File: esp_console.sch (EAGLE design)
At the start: 37 parts, among them IC1 74AHC1G04DBV, IC2 UA78M05DCY, J2 10118193-0001LF, Q1 12mhz, Q2 ON_SEMICONDUCTOR_BC849BLT1GON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, Q3 ON_SEMICONDUCTOR_BC849BLT1GON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, SW1 OS102011MA1Q

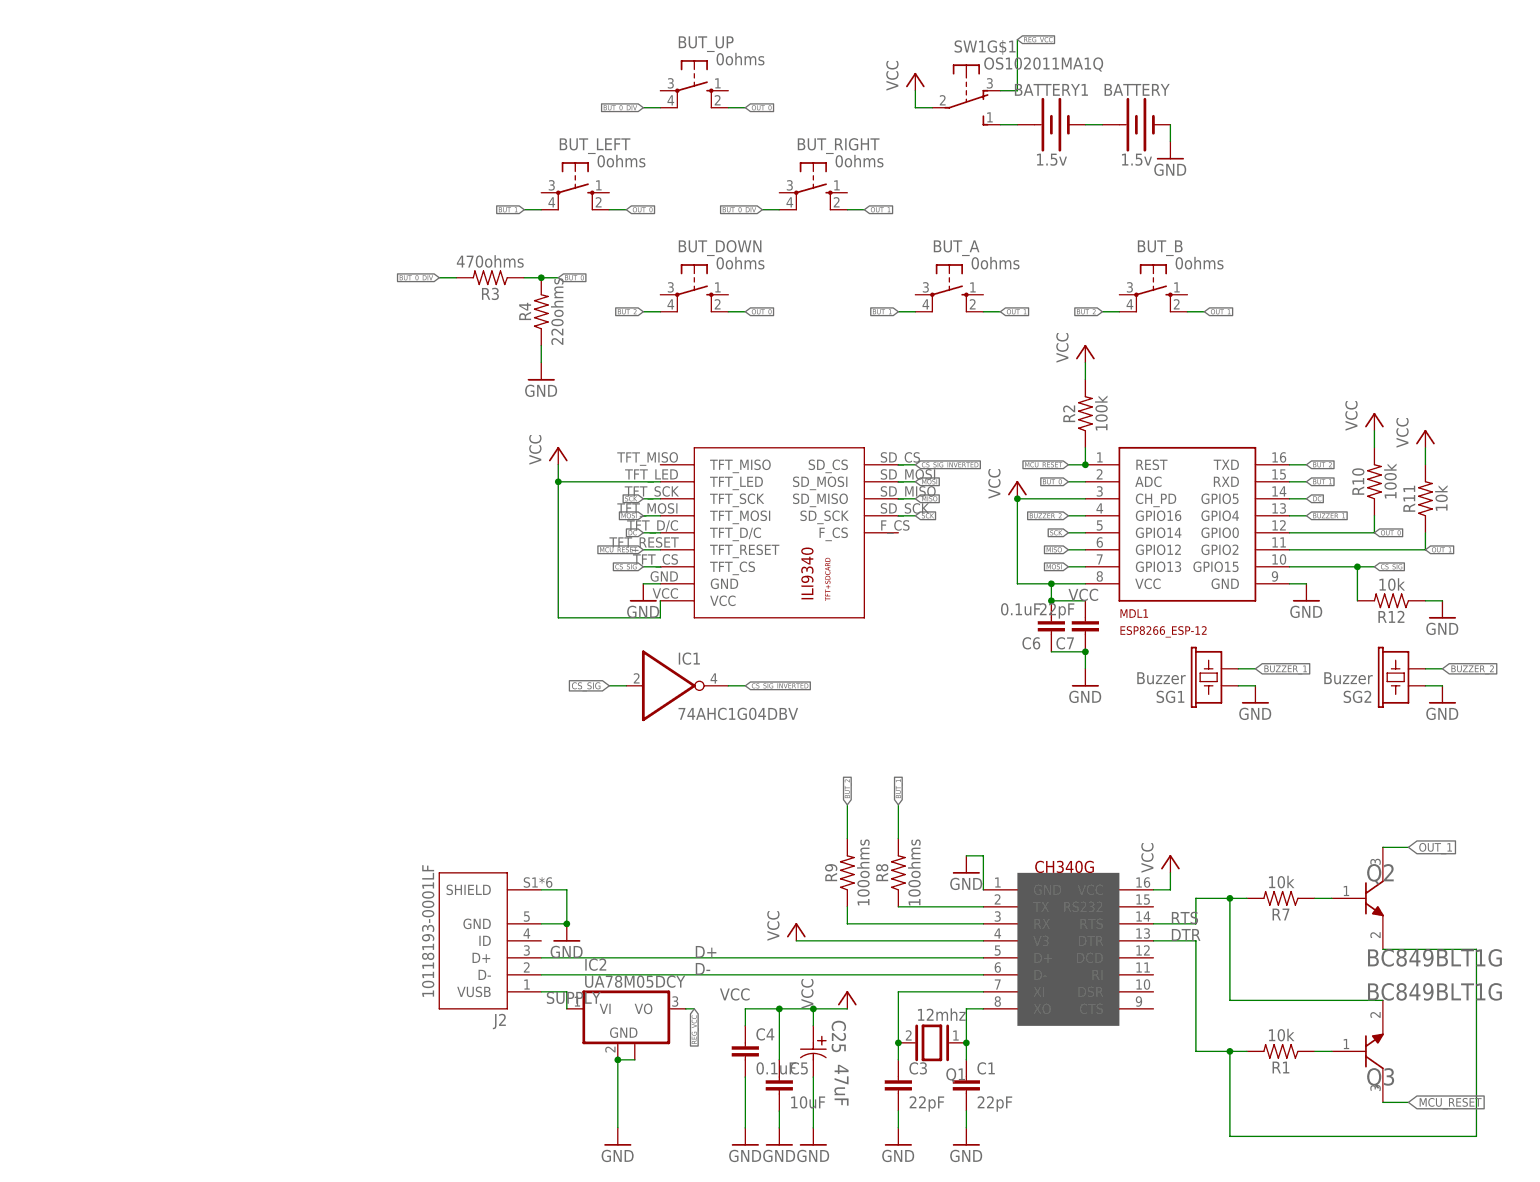
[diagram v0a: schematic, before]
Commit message: Updated design to 8 buttons
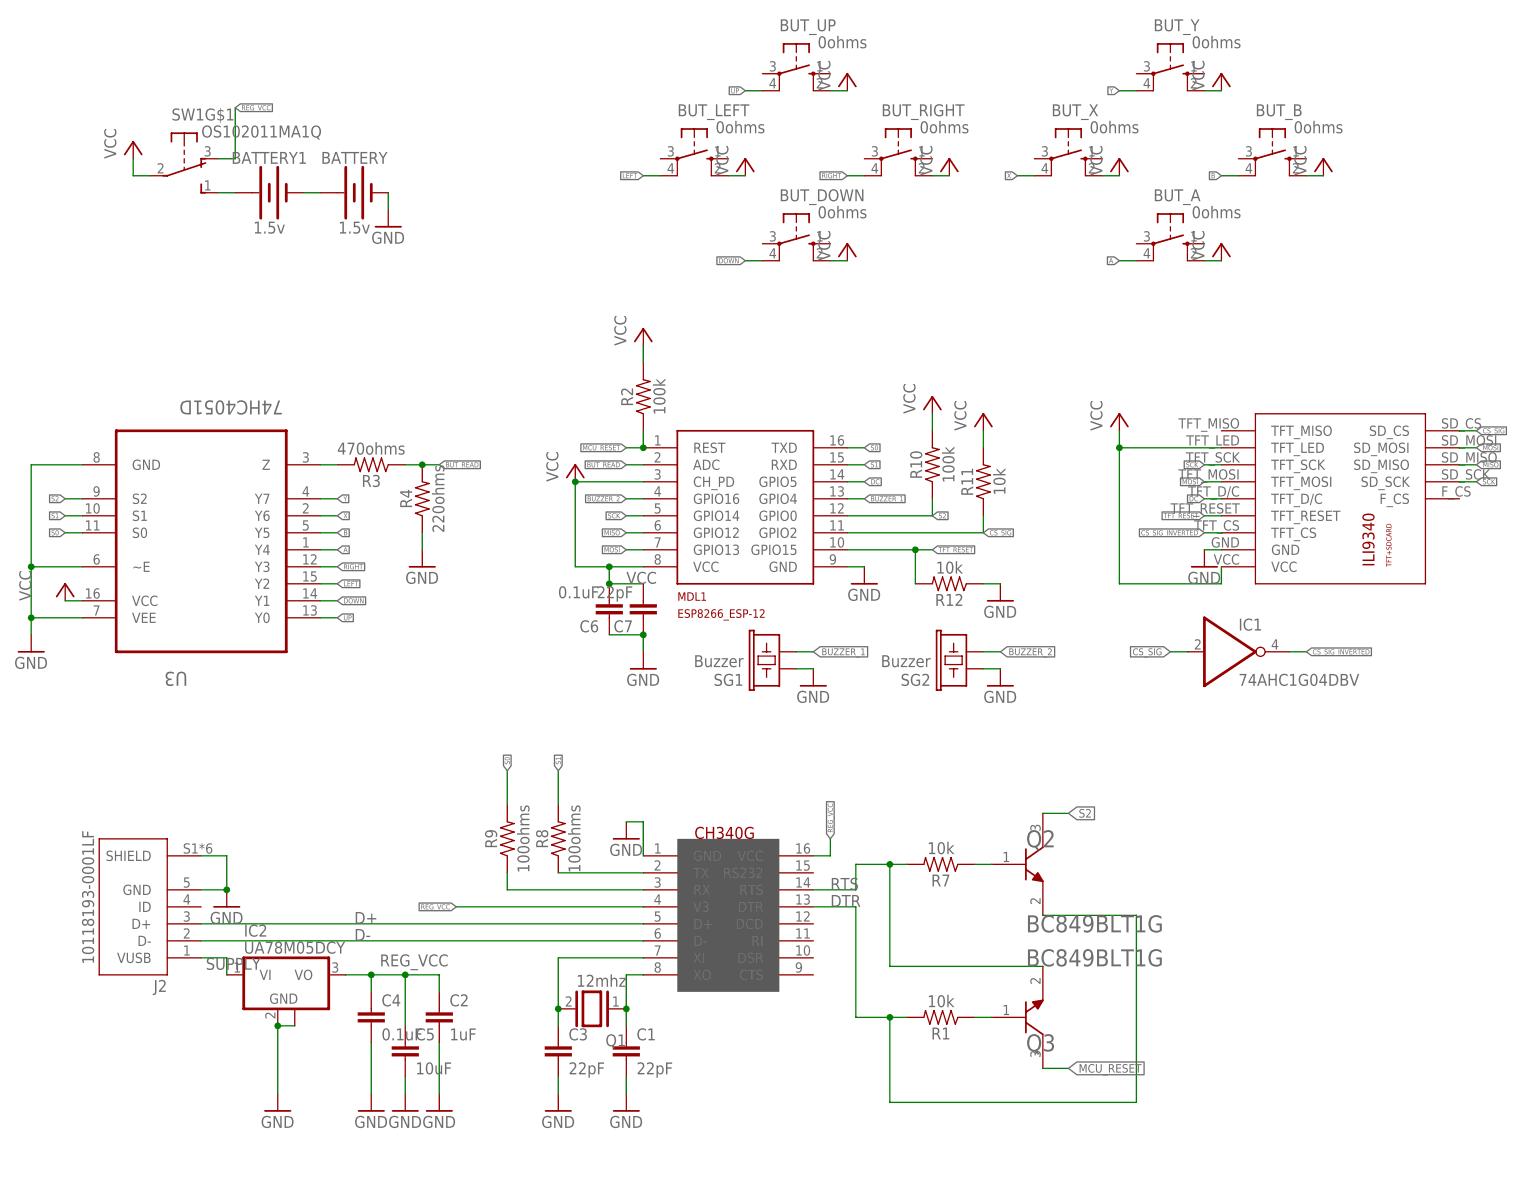
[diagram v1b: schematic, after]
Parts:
- removed C25: 47uF, Panasonic-EEEFK_EEEFP:EEE-FK1C471P-CASE-F
- added BUT_X, BUT_Y: 0ohms, switch-omron:10-XX
- added C2: 1uF, rcl:C-EUC0603
- added U3: 74HC4051D, 74HC4051D:74HC4051D
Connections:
- net BUT_0 renamed BUT_READ
- removed net BUT_0_DIV: BUT_RIGHT.P1, BUT_UP.P1, R3.2
- removed net BUT_1: BUT_A.P1, BUT_LEFT.P1, MDL1.RXD, R8.2
- removed net BUT_2: BUT_B.P1, BUT_DOWN.P1, MDL1.TXD, R9.2
- removed net OUT_0: BUT_DOWN.S1, BUT_LEFT.S1, BUT_UP.S1, MDL1.GPIO0, R10.1
- removed net OUT_1: BUT_A.S1, BUT_B.S1, BUT_RIGHT.S1, MDL1.GPIO2, Q2.C, R11.1
- new net A: BUT_A.P1, U3.Y4
- new net B: BUT_B.P1, U3.Y5
- new net BUT_READ_3V3: R3.2, U3.Z
- new net DOWN: BUT_DOWN.P1, U3.Y1
- new net LEFT: BUT_LEFT.P1, U3.Y2
- new net RIGHT: BUT_RIGHT.P1, U3.Y3
- new net S0: MDL1.TXD, R9.2, U3.S0
- new net S1: MDL1.RXD, R8.2, U3.S1
- new net S2: MDL1.GPIO0, Q2.C, R10.1, U3.S2
- new net TFT_RESET: MDL1.GPIO15, R12.2, U$2.TFT_RESET
- new net UP: BUT_UP.P1, U3.Y0
- new net X: BUT_X.P1, U3.Y6
- new net Y: BUT_Y.P1, U3.Y7
- net CS_SIG: now also MDL1.GPIO2, R11.1, U$2.SD_CS; no longer MDL1.GPIO15, R12.2, U$2.TFT_CS
- net CS_SIG_INVERTED: now also U$2.TFT_CS; no longer U$2.SD_CS
- net GND: now also C2.2, U3.GND, U3.VEE, U3.~E; no longer C25.2
- net MCU_RESET: no longer U$2.TFT_RESET
- net REG_VCC: now also C2.1, C4.1, C5.1, U$1.V3, U$1.VCC
- net VCC: now also BUT_A.S1, BUT_B.S1, BUT_DOWN.S1, BUT_LEFT.S1, BUT_RIGHT.S1, BUT_UP.S1, BUT_X.S1, BUT_Y.S1, U3.VCC; no longer C25.1, C4.1, C5.1, U$1.V3, U$1.VCC
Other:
- moved on the sheet: BATTERY, BATTERY1, BUT_A, BUT_B, BUT_DOWN, BUT_LEFT, BUT_RIGHT, BUT_UP, C1, C3, C4, C5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

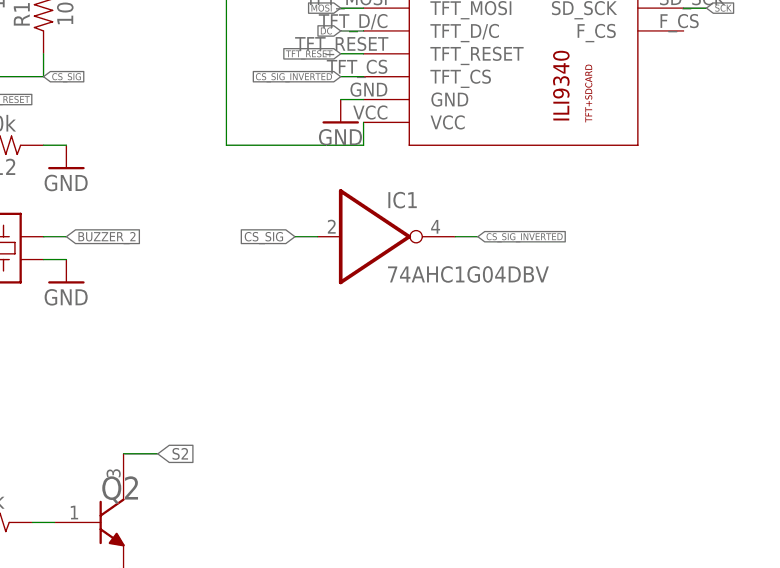
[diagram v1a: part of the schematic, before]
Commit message: Added pullup to inverter, new gerbers
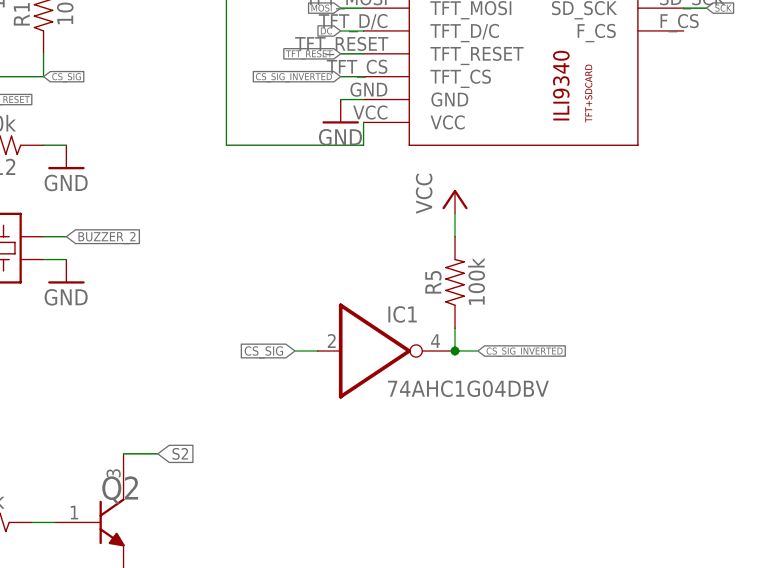
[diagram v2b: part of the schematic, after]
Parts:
- added R5: 100k, SparkFun-Resistors:10KOHM-0603-1/10W-1%
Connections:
- net CS_SIG_INVERTED: now also R5.1
- net VCC: now also R5.2
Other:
- moved on the sheet: IC1
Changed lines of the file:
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@@
 <part name="P+18" library="supply1" library_urn="urn:adsk.eagle:library:371" deviceset="VCC" device=""/>
 <part name="C2" library="rcl" library_urn="urn:adsk.eagle:library:334" deviceset="C-EU" device="C0603" package3d_urn="urn:adsk.eagle:package:23616/2" value="1uF"/>
+<part name="R5" library="SparkFun-Resistors" library_urn="urn:adsk.eagle:library:532" deviceset="10KOHM" device="-0603-1/10W-1%" package3d_urn="urn:adsk.eagle:package:39650/1" value="100k"/>
+<part name="P+1" library="supply1" library_urn="urn:adsk.eagle:library:371" deviceset="VCC" device=""/>
 </parts>
 <sheets>
@@
 <attribute name="VALUE" x="-86.36" y="-35.56" size="1.778" layer="96"/>
 </instance>
-<instance part="IC1" gate="A" x="35.56" y="-45.72" smashed="yes">
-<attribute name="NAME" x="38.1" y="-42.545" size="1.778" layer="95"/>
-<attribute name="VALUE" x="38.1" y="-50.8" size="1.778" layer="96"/>
+<instance part="IC1" gate="A" x="35.56" y="-58.42" smashed="yes">
+<attribute name="NAME" x="38.1" y="-55.245" size="1.778" layer="95"/>
+<attribute name="VALUE" x="38.1" y="-63.5" size="1.778" layer="96"/>
 </instance>
 <instance part="U3" gate="A" x="-116.84" y="-33.02" smashed="yes" rot="MR180">
@@
 <attribute name="NAME" x="-79.756" y="-98.679" size="1.778" layer="95"/>
 <attribute name="VALUE" x="-79.756" y="-103.759" size="1.778" layer="96"/>
+</instance>
+<instance part="R5" gate="G$1" x="45.72" y="-50.8" smashed="yes" rot="R90">
+<attribute name="NAME" x="44.196" y="-50.8" size="1.778" layer="95" font="vector" rot="R90" align="bottom-center"/>
+<attribute name="VALUE" x="47.244" y="-50.8" size="1.778" layer="96" font="vector" rot="R90" align="top-center"/>
+</instance>
+<instance part="P+1" gate="VCC" x="45.72" y="-40.64" smashed="yes">
+<attribute name="VALUE" x="43.18" y="-43.18" size="1.778" layer="96" rot="R90"/>
 </instance>
 </instances>
@@
 <pinref part="P+18" gate="VCC" pin="VCC"/>
 </segment>
+<segment>
+<wire x1="45.72" y1="-45.72" x2="45.72" y2="-43.18" width="0.1524" layer="91"/>
+<pinref part="R5" gate="G$1" pin="2"/>
+<pinref part="P+1" gate="VCC" pin="VCC"/>
+</segment>
 </net>
 <net name="MCU_RESET" class="0">
@@
 <segment>
 <pinref part="IC1" gate="A" pin="I"/>
-<wire x1="30.48" y1="-45.72" x2="27.94" y2="-45.72" width="0.1524" layer="91"/>
-<label x="27.94" y="-45.72" size="1.016" layer="95" rot="R180" xref="yes"/>
+<wire x1="30.48" y1="-58.42" x2="27.94" y2="-58.42" width="0.1524" layer="91"/>
+<label x="27.94" y="-58.42" size="1.016" layer="95" rot="R180" xref="yes"/>
 </segment>
 <segment>
@@
 <segment>
 <pinref part="IC1" gate="A" pin="O"/>
-<wire x1="45.72" y1="-45.72" x2="48.26" y2="-45.72" width="0.1524" layer="91"/>
-<label x="48.26" y="-45.72" size="0.762" layer="95" xref="yes"/>
-</segment>
-<segment>
+<wire x1="45.72" y1="-58.42" x2="48.26" y2="-58.42" width="0.1524" layer="91"/>
+<label x="48.26" y="-58.42" size="0.762" layer="95" xref="yes"/>
+<pinref part="R5" gate="G$1" pin="1"/>
+<wire x1="45.72" y1="-55.88" x2="45.72" y2="-58.42" width="0.1524" layer="91"/>
+<junction x="45.72" y="-58.42"/>
+</segment>
+<segment>
